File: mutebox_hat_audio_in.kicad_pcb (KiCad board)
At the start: 2 copper layers, 65 x 56 mm, 41 parts, among them J1 GPIO, J2 PLR237/T10BK, U1 CAT24C256, U2 74LVC157, U3 PCM1862DBT, U4 DIR9001PW, Y1 12.288 MHz

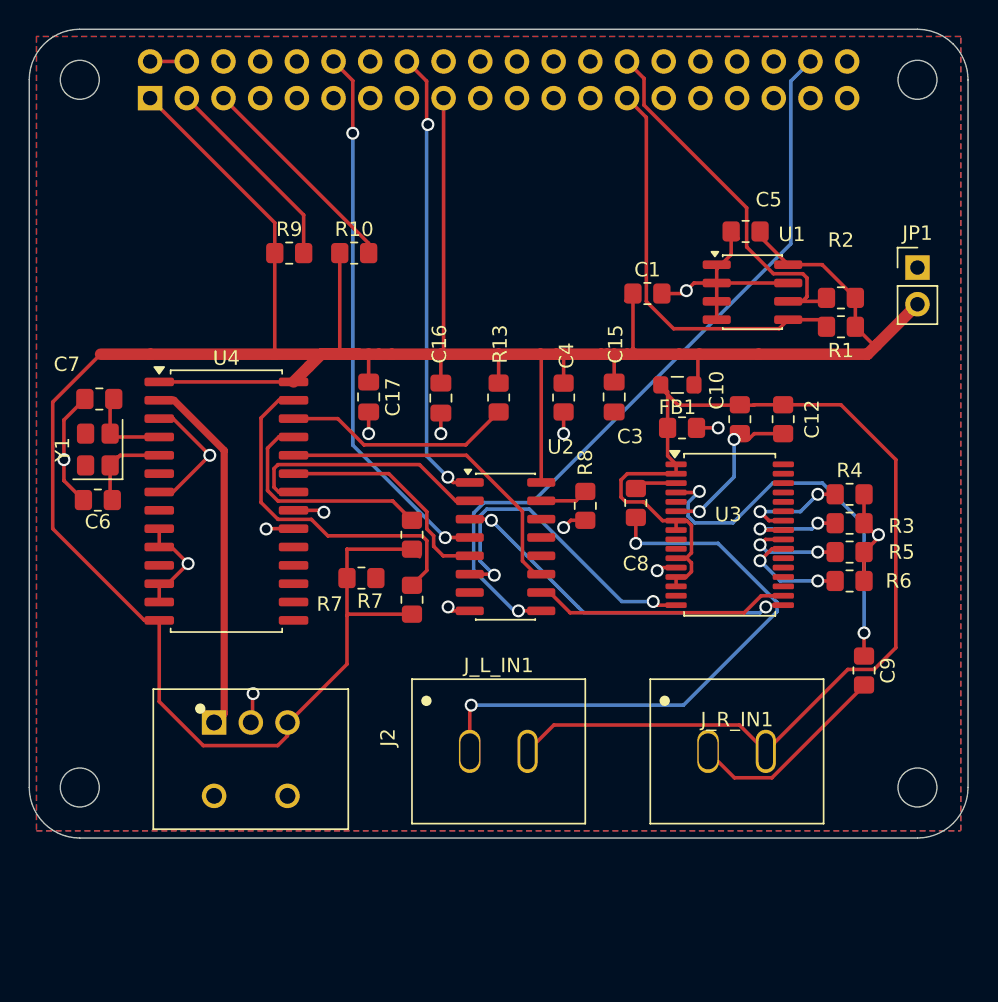
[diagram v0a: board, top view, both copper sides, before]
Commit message: Changed DIN connections
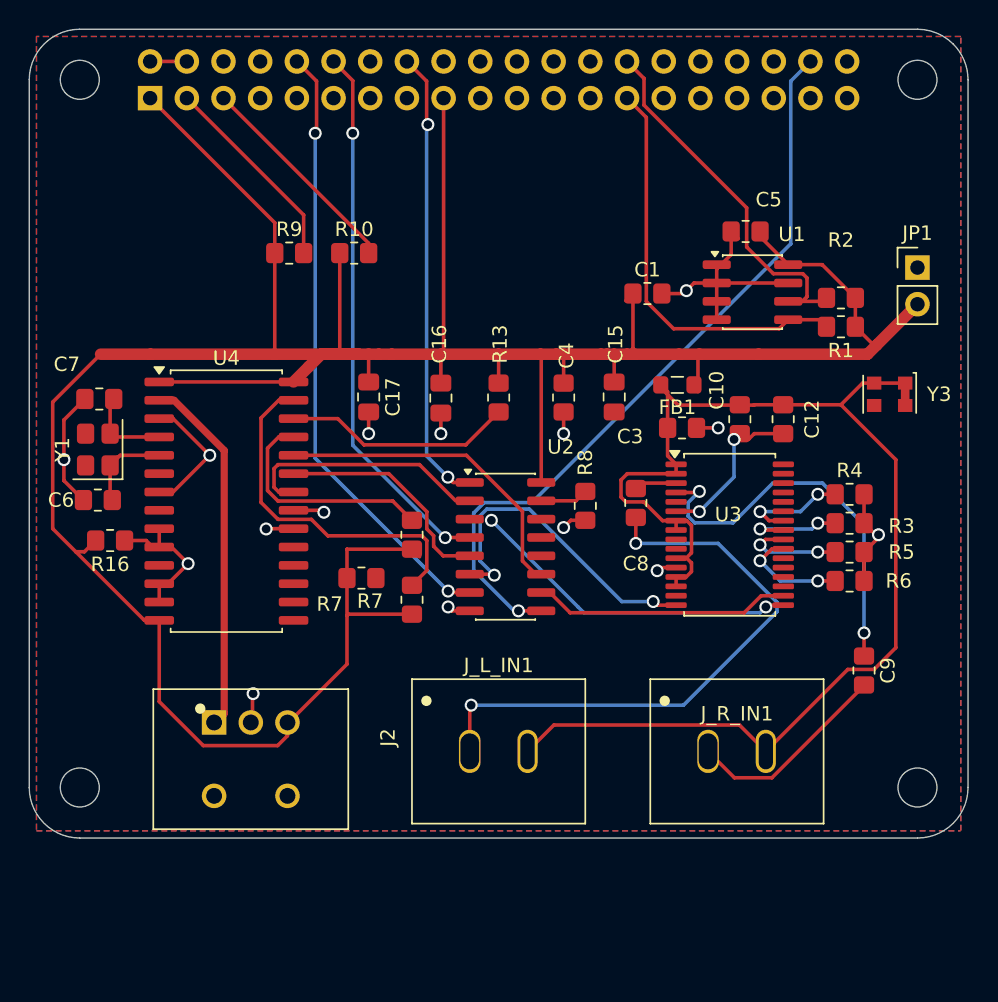
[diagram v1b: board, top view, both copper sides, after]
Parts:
- added R16: 10k, Resistor_SMD:R_0805_2012Metric_Pad1.20x1.40mm_HandSolder, F.Cu at (105.6, 79.4)
- added Y3: XO32, Oscillator:Oscillator_SMD_EuroQuartz_XO32-4Pin_3.2x2.5mm, F.Cu at (159.6, 69.3)
- C8: value 1uF -> 1uF (film preferred)
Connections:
- J1 pad 10: /GPIO15/RXD0 -> I2S_LRCLK
- J1 pad 35: I2S_SDIN -> I2S_LRCLK
- R7 pad 1: +3V3 -> Net-(U4-~{RST})
- R7 pad 2: Net-(U4-~{RST}) -> +3V3
- U2 pad 10: ADC_SDOUT -> TOSLINK_DOUT
- U2 pad 11: TOSLINK_DOUT -> ADC_SDOUT
- U2 pad 2: TOSLINK_BCLK -> ADC_BCLK
- U2 pad 3: ADC_BCLK -> TOSLINK_BCLK
- U2 pad 5: TOSLINK_LRCLK -> ADC_LRCLK
- U2 pad 6: ADC_LRCLK -> TOSLINK_LRCLK
- U3 pad 15: unconnected-(U3-SCKI-Pad15) -> Net-(U3-SCKI)
- U4 pad 10: GND -> Net-(U4-PD0)
- U4 pad 12: GND -> Net-(U4-FMT0)
- U4 pad 13: GND -> Net-(U4-FMT1)
- U4 pad 5: Net-(U4-XO) -> unconnected-(U4-XO-Pad5)
- U4 pad 9: GND -> Net-(U4-PD1)
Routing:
- net I2S_LRCLK: track 0.00 -> 42.6 mm, vias 0 -> 2
- net 3V3_A: track 86.2 -> 92.8 mm
- net Net-(U4-PD0): track 0.00 -> 2.14 mm
- net +3V3: track 222.4 -> 224.1 mm
- net ADC_BCLK: track 24.6 -> 23.2 mm
- net TOSLINK_BCLK: track 17.5 -> 16.5 mm
- net GND: track 65.8 -> 65.0 mm

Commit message: More routing on PCB
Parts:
- added C2: C, Capacitor_SMD:C_0805_2012Metric_Pad1.18x1.45mm_HandSolder, F.Cu at (156.0, 68.8)
- added R14: 33, Resistor_SMD:R_0805_2012Metric_Pad1.20x1.40mm_HandSolder, F.Cu at (161.8, 73.7)
- added R15: 10k, Resistor_SMD:R_0805_2012Metric_Pad1.20x1.40mm_HandSolder, F.Cu at (104.8, 63.4)
- added R17: 10k, Resistor_SMD:R_0805_2012Metric_Pad1.20x1.40mm_HandSolder, F.Cu at (105.2, 78.4)
- added R18: 10k, Resistor_SMD:R_0805_2012Metric_Pad1.20x1.40mm_HandSolder, F.Cu at (105.6, 83.8)
- added R19: 10k, Resistor_SMD:R_0805_2012Metric_Pad1.20x1.40mm_HandSolder, F.Cu at (105.6, 86.2)
- moved C10 1.46 mm to (148.8, 69.6)
- moved C12 1.46 mm to (151.8, 69.6)
- moved Y3 1.35 mm to (160.9, 69.3)
- moved R16 1.03 mm to (105.2, 80.3)
- moved R7 0.51 mm to (126.6, 83.0), turned to -90 degrees
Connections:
- C10 pad 1: 3V3_A -> /VREF
- C10 pad 2: Net-(U3-VREF) -> GND
- C12 pad 1: 3V3_A -> /VREF
- C12 pad 2: Net-(U3-VREF) -> GND
- J1 pad 10: I2S_LRCLK -> unconnected-(J1-Pin_10-Pad10)
- J1 pad 16: SRC_SEL -> GPIO23_OPT_LOCK
- J_L_IN1 pad 2: 3V3_A -> /VREF
- J_R_IN1 pad 2: 3V3_A -> /VREF
- U2 pad 1: SRC_SEL -> GPIO23_OPT_LOCK
- U3 pad 1: 3V3_A -> /VREF
- U3 pad 2: 3V3_A -> /VREF
- U3 pad 6: Net-(U3-VREF) -> /VREF
- U3 pad 7: 3V3_A -> GND
- Y3 pad 1: 3V3_A -> GND
- Y3 pad 2: 3V3_A -> GND
- Y3 pad 4: 3V3_A -> GND
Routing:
- net 3V3_A: track 92.8 -> 9.84 mm
- net /VREF: track 0.00 -> 78.2 mm
- net GND: track 65.0 -> 103.9 mm
- net Net-(U3-SCKI): track 0.00 -> 35.0 mm, vias 0 -> 2
- net GPIO23_OPT_LOCK: track 0.00 -> 34.2 mm, vias 0 -> 3
- net SRC_SEL: track 31.7 -> 0.00 mm, vias 2 -> 0
- net Net-(U3-VREF): track 11.2 -> 0.00 mm, vias 2 -> 0
- net +3V3: track 224.1 -> 234.9 mm
- net Net-(U4-FMT0): track 0.00 -> 8.16 mm
- net Net-(U4-XO): track 6.86 -> 2.46 mm
- net Net-(Y3-OUT): track 0.00 -> 3.42 mm
- net Net-(U4-PD1): track 0.00 -> 2.87 mm
- net I2S_LRCLK: track 42.6 -> 45.1 mm
- net Net-(U4-FMT1): track 0.00 -> 2.26 mm
- net Net-(U4-PD0): track 2.14 -> 3.01 mm
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
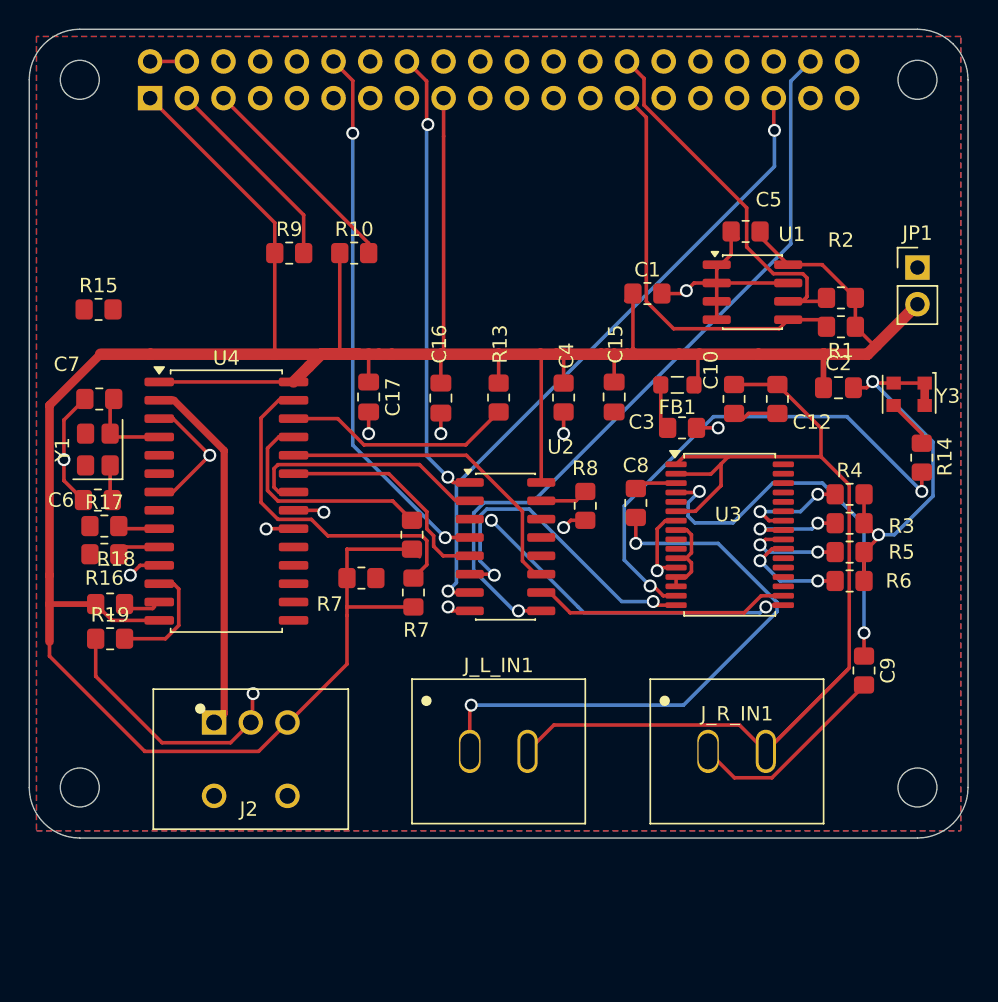
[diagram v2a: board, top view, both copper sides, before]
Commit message: Fixed all routes but TOSLINK footprint
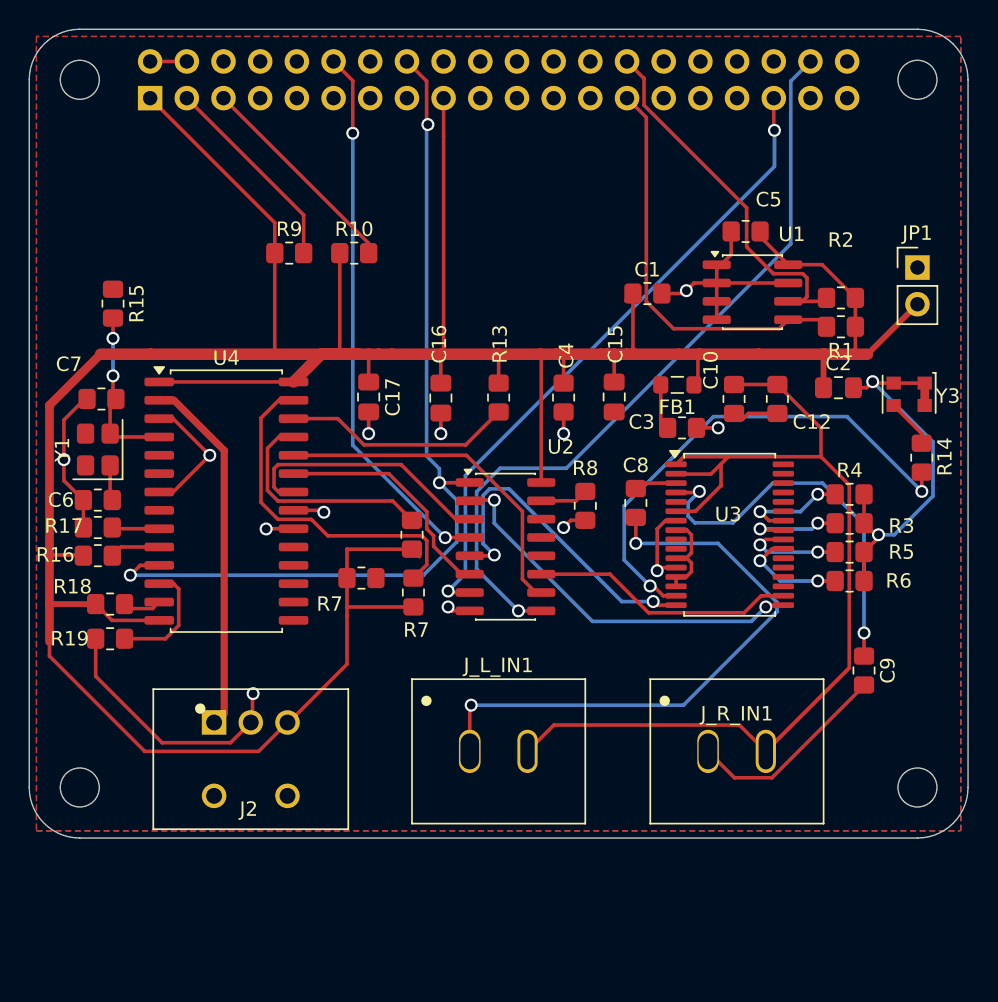
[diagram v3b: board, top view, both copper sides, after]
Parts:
- moved R15 1.08 mm to (105.8, 63.0), turned to -90 degrees
- moved R16 0.46 mm to (104.8, 80.5)
- moved R17 0.46 mm to (104.8, 78.5)
- moved C7 0.15 mm to (105.0, 69.6)
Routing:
- net GPIO23_OPT_LOCK: track 34.2 -> 63.0 mm
- net Net-(U4-XI): track 6.61 -> 12.3 mm, vias 0 -> 2
- net ADC_BCLK: track 23.2 -> 26.6 mm
- net GND: track 103.9 -> 106.4 mm
- net +3V3: track 234.9 -> 237.1 mm
- net TOSLINK_DOUT: track 22.6 -> 24.4 mm
- net TOSLINK_BCLK: track 16.5 -> 18.0 mm
- net I2S_DOUT: track 52.8 -> 53.4 mm
- net TOSLINK_LRCLK: track 15.7 -> 16.2 mm

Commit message: Fixed footprint for ADC chip (PCM1862).  Fixed more issues.
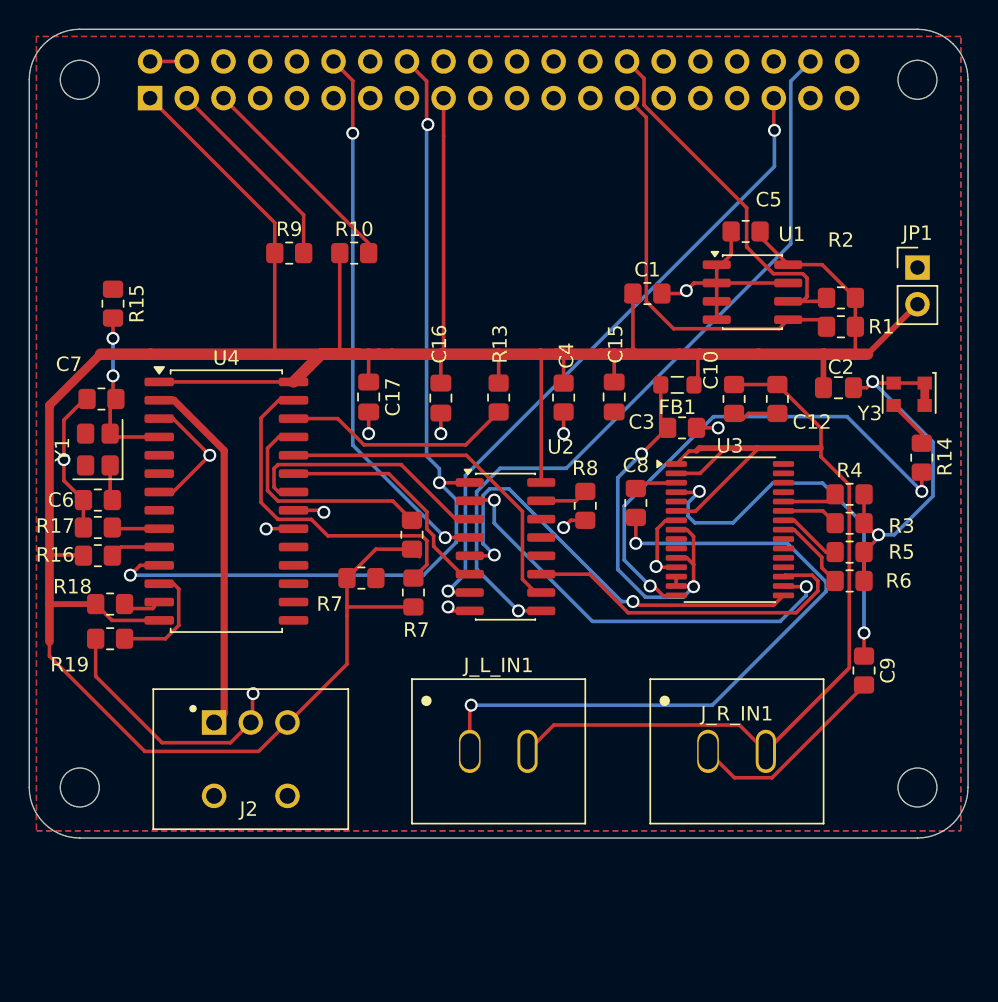
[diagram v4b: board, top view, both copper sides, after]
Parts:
- U3: footprint Package_SO:TSSOP-32_6.1x11mm_P0.65mm -> Package_SO:TSSOP-30_6.1x9.7mm_P0.65mm
- moved U3 0.35 mm to (148.5, 78.7)
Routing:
- net 3V3_A: track 9.84 -> 28.2 mm, vias 0 -> 2
- net ADC_LRCLK: track 22.5 -> 30.2 mm
- net Net-(J_L_IN1-In): track 41.0 -> 47.8 mm
- net ADC_SDOUT: track 18.3 -> 24.1 mm
- net ADC_BCLK: track 26.6 -> 30.7 mm
- net MD0: track 7.57 -> 3.78 mm, vias 2 -> 0
- net MODE_MS: track 7.01 -> 3.93 mm, vias 2 -> 0
- net /VREF: track 78.2 -> 81.0 mm
- net MODE_FMT0: track 7.17 -> 4.49 mm, vias 2 -> 0
- net MODE_FMT1: track 7.73 -> 5.46 mm, vias 2 -> 0
- net +3V3: track 237.1 -> 235.9 mm

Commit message: Added symbol and footprint for PLR237/T10BK Toslink
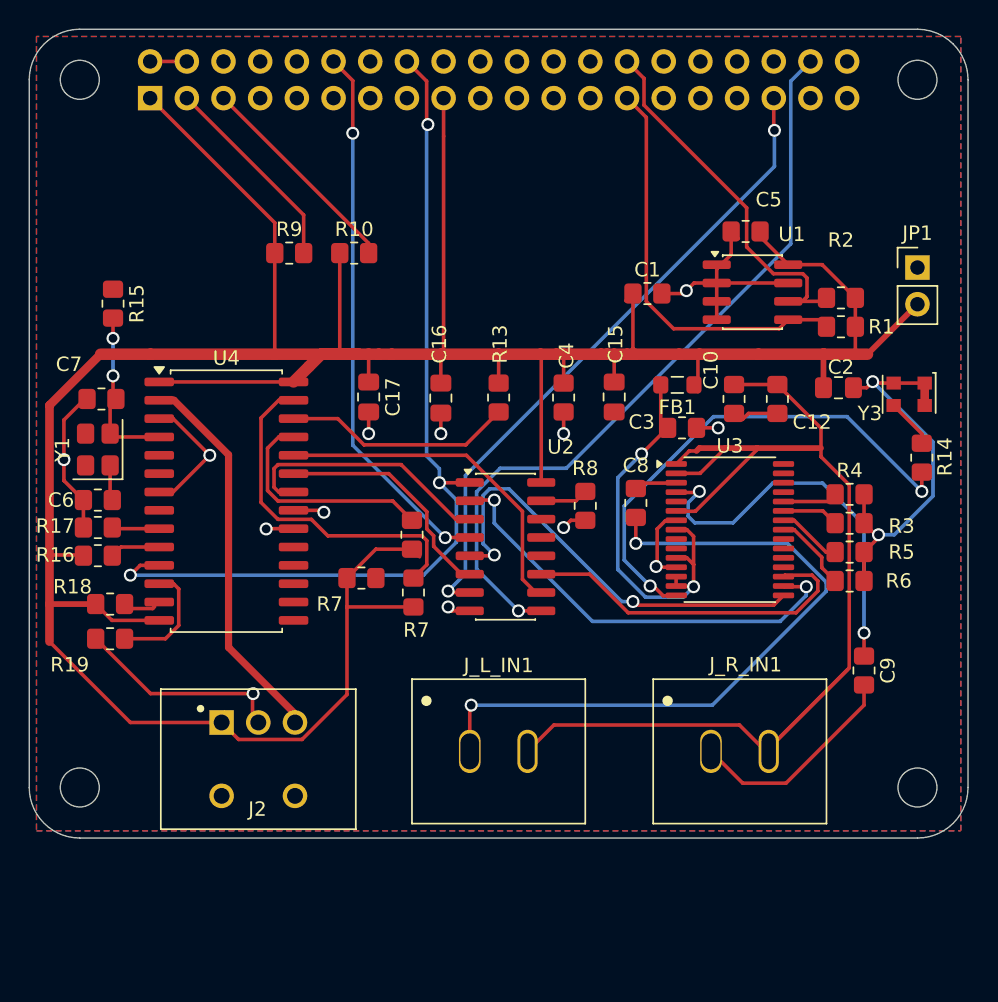
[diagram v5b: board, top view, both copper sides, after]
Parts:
- moved J2 0.52 mm to (115.9, 94.5)
- moved J_R_IN1 0.20 mm to (149.2, 94.0)
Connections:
- J2 pad 1: /Audio Inputs/SPDIF_IN -> +3V3
- J2 pad 3: +3V3 -> /Audio Inputs/SPDIF_IN
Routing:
- net GND: track 106.2 -> 102.8 mm
- net /Audio Inputs/SPDIF_IN: track 25.0 -> 26.8 mm
- net +3V3: track 235.9 -> 236.8 mm
- net Net-(J_R_IN1-In): track 14.2 -> 15.1 mm

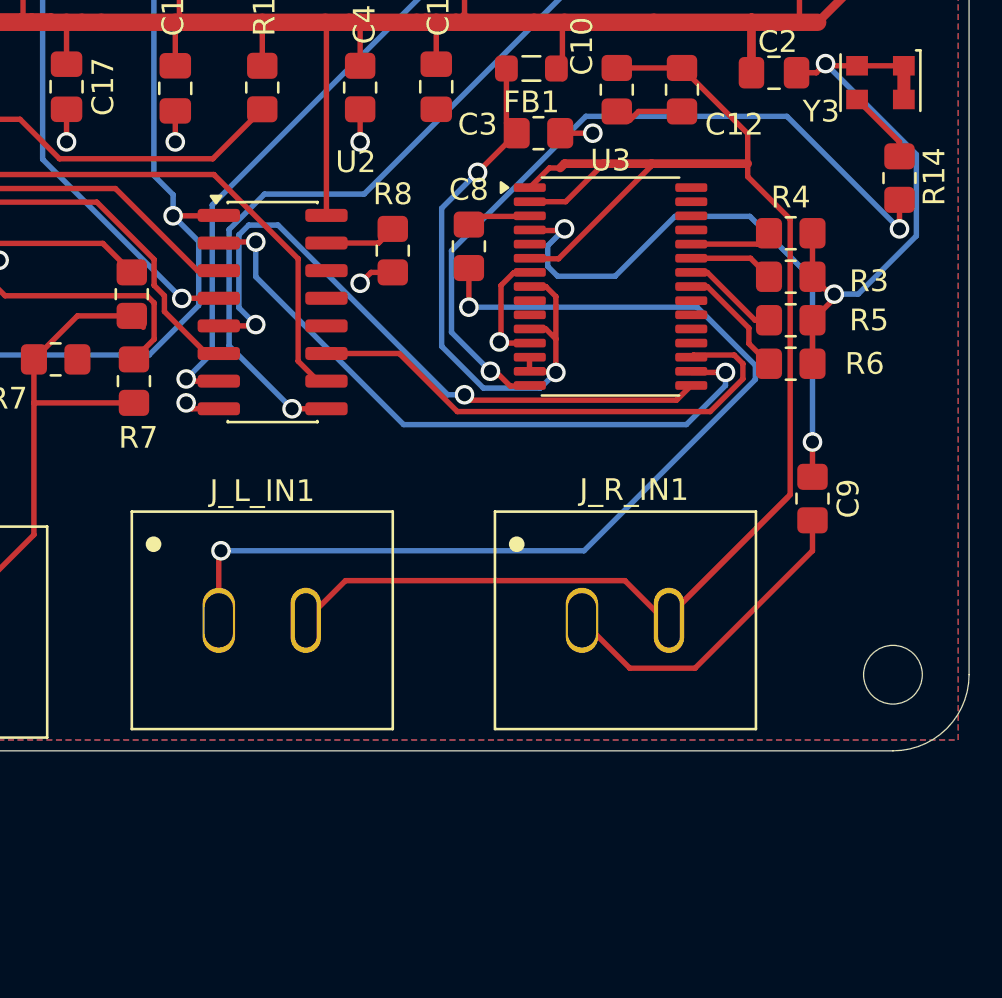
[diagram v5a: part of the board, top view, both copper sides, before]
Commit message: Fixed RCA Jack symbols and footprints
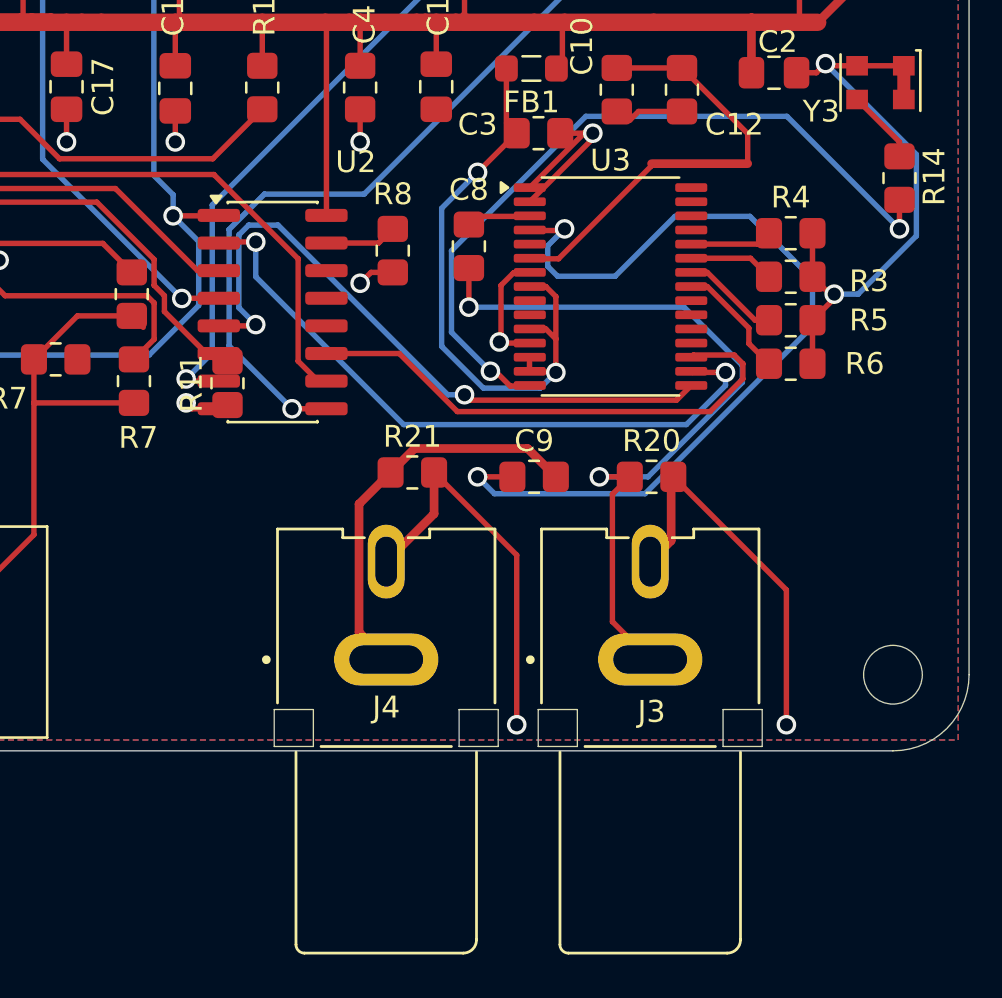
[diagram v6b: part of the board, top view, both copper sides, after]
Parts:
- removed J_L_IN1, J_R_IN1: Conn_Coaxial, Connector_Audio:RCJ-043
- added J3: RCJ-042, RCJ-042:CUI_RCJ-042, F.Cu at (150.3, 99.8)
- added J4: RCJ-042, RCJ-042:CUI_RCJ-042, F.Cu at (138.2, 99.8)
- added R11: 100k, Resistor_SMD:R_0805_2012Metric_Pad1.20x1.40mm_HandSolder, F.Cu at (130.9, 83.1)
- added R20: 100k, Resistor_SMD:R_0805_2012Metric_Pad1.20x1.40mm_HandSolder, F.Cu at (150.4, 87.4)
- added R21: 100k, Resistor_SMD:R_0805_2012Metric_Pad1.20x1.40mm_HandSolder, F.Cu at (139.4, 87.2)
- moved C9 12.8 mm to (145.0, 87.4), turned to 0 degrees
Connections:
- U3 pad 1: /VREF -> GND
- U3 pad 2: /VREF -> GND
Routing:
- net /VREF: track 81.0 -> 20.6 mm
- net GND: track 102.8 -> 147.2 mm, vias 15 -> 17
- net Net-(U3-VINR1/VIN2P): track 27.5 -> 41.1 mm
- net Net-(C8-Pad2): track 47.8 -> 35.6 mm
- net Net-(C9-Pad2): track 15.1 -> 18.3 mm
